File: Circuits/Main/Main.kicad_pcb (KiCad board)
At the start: 2 copper layers, 33 parts, among them CON1 BARREL_JACK, P1 led_stop, P10 toEncoder_MotorL, P11 toEncoder_motorR, P12 conn_resetButton, P13 conn_resetButton, P2 led_droite_face, P3 led_droite_cote, P4 led_gauche_face, P5 led_gauche_cote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

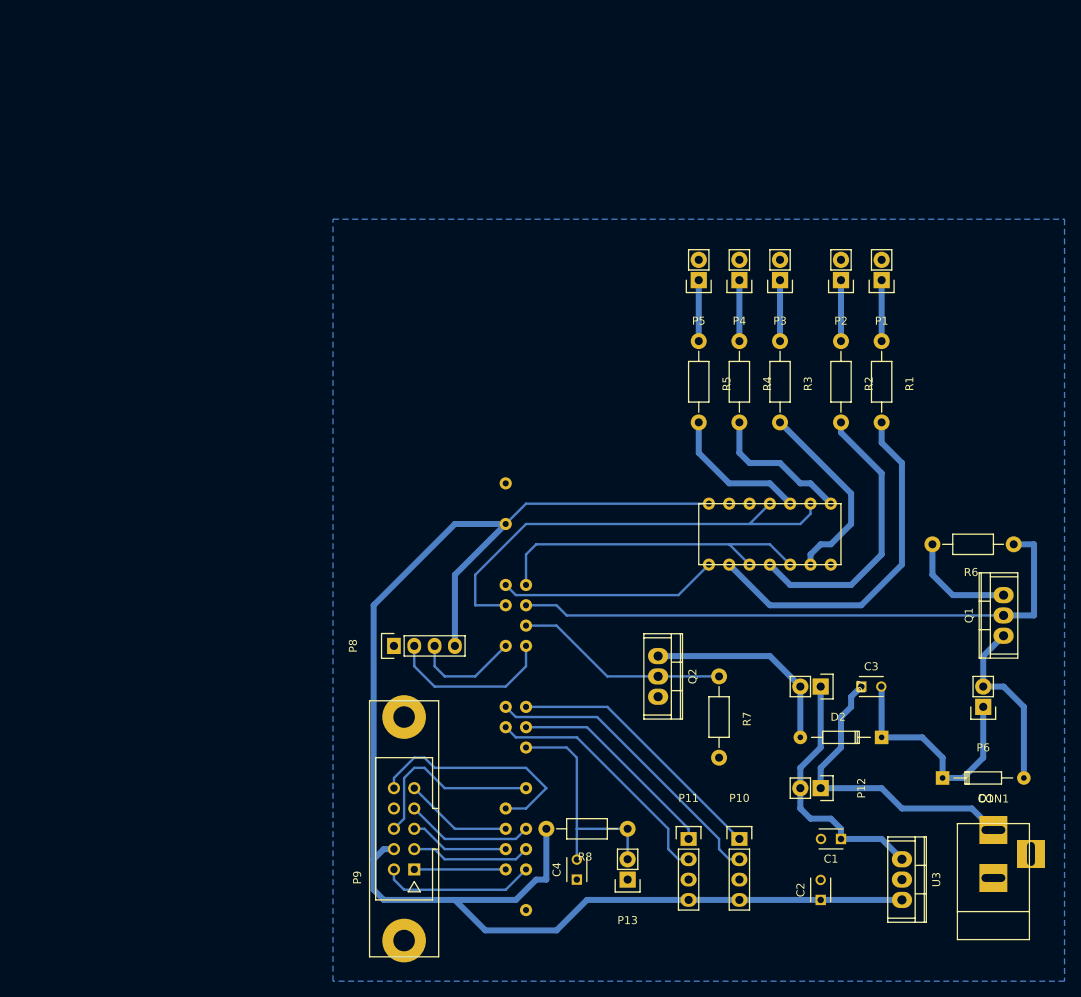
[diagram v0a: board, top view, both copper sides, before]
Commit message: Ajout de la carte principale (schemas + gerbers) et intégration
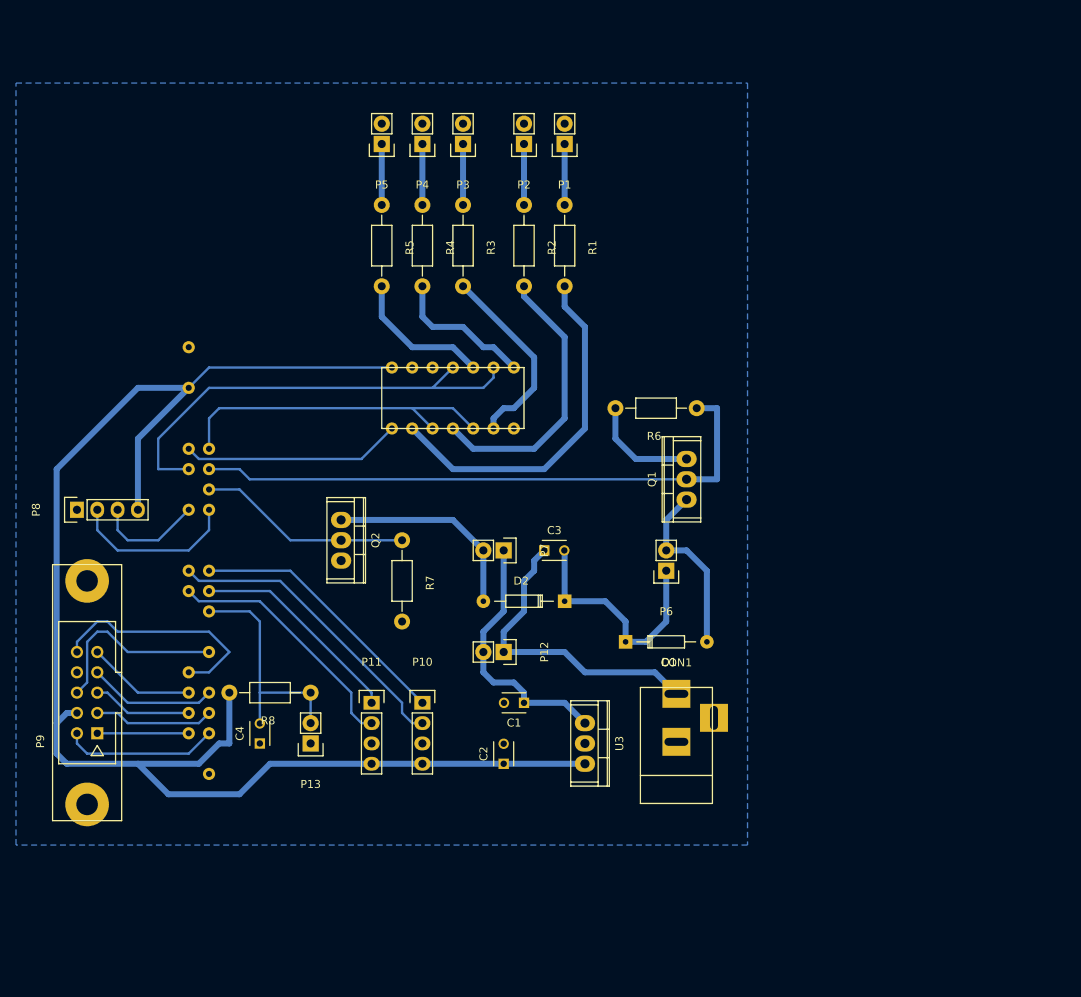
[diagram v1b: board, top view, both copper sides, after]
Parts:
- moved C3 43.1 mm to (92.5, 80.8)
- moved CON1 43.1 mm to (109.0, 104.9)
- moved D1 43.1 mm to (102.6, 92.2)
- moved D2 43.1 mm to (95.0, 87.1)
- moved P1 43.1 mm to (95.0, 30.0)
- moved P10 43.1 mm to (77.2, 99.8)
- moved P4 43.1 mm to (77.2, 30.0)
- moved P5 43.1 mm to (72.1, 30.0)
- moved Q1 43.1 mm to (110.2, 71.9)
- moved Q2 43.1 mm to (67.1, 79.5)
- moved R1 43.1 mm to (95.0, 37.6)
- moved R4 43.1 mm to (77.2, 37.6)
- moved R5 43.1 mm to (72.1, 37.6)
- moved R6 43.1 mm to (111.5, 63.0)
- moved P13 43.1 mm to (63.2, 104.9)
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
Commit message: Ameliorations cartes + rapport
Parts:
- P1: value led_stop -> toEncoder_MotorL; footprint Pin_Headers:Pin_Header_Straight_1x02 -> Pin_Headers:Pin_Header_Straight_1x04
- P10: value toEncoder_MotorL -> conn_moteur_gauche; footprint Pin_Headers:Pin_Header_Straight_1x04 -> Pin_Headers:Pin_Header_Straight_1x02
- P11: value toEncoder_motorR -> ultrasonicSensor
- P12: value conn_resetButton -> HE10-10; footprint Pin_Headers:Pin_Header_Straight_1x02 -> Connect:he10-10d
- P2: value led_droite_face -> led_stop
- P3: value led_droite_cote -> toEncoder_motorR; footprint Pin_Headers:Pin_Header_Straight_1x02 -> Pin_Headers:Pin_Header_Straight_1x04
- P4: value led_gauche_face -> led_droite_face
- P5: value led_gauche_cote -> led_droite_cote
- P6: value conn_moteur_droit -> led_gauche_face
- P7: value conn_moteur_gauche -> led_gauche_cote
- P8: value ultrasonicSensor -> conn_moteur_droit; footprint Pin_Headers:Pin_Header_Straight_1x04 -> Pin_Headers:Pin_Header_Straight_1x02
- P9: value HE10-10 -> conn_switchOnOff; footprint Connect:he10-10d -> Pin_Headers:Pin_Header_Straight_1x02
- U3: footprint Power_Integrations:TO-220 -> MES_EMPREINTES:voltageRegulator5v
- moved P6 86.3 mm to (42.5, 26.7), turned to 270 degrees
- moved P7 66.4 mm to (42.5, 31.8)
- moved P8 59.0 mm to (92.7, 69.2), turned to 270 degrees
- moved P11 53.3 mm to (42.5, 54.6), turned to 180 degrees
- moved P9 52.5 mm to (85.1, 81.9), turned to 270 degrees
- moved P12 45.6 mm to (43.8, 80.0), turned to 90 degrees
- moved P13 44.9 mm to (54.0, 61.0), turned to 90 degrees
- moved R8 41.9 mm to (56.5, 57.1)
- moved R6 41.7 mm to (78.1, 38.1), turned to 0 degrees
- moved C4 40.2 mm to (54.0, 64.8), turned to 0 degrees
- moved U3 39.8 mm to (60.3, 90.8), turned to 180 degrees
- moved D1 38.9 mm to (100.3, 53.3), turned to 90 degrees
- moved P3 35.1 mm to (71.8, 63.5), turned to 0 degrees
- moved Q1 34.4 mm to (95.9, 40.6)
- moved R4 32.1 mm to (47.0, 26.7), turned to 0 degrees
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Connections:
- C2 pad 1: 5v_Bat -> +BATT
- C2 pad 2: gnd -> batt
- C3 pad 1: +BATT -> 5v_Bat
- C3 pad 2: batt -> gnd
- P1 pad 1: Net-(P1-Pad1) -> toEncoder1B
- P1 pad 2: gnd -> toEncoder1A
- P10 pad 1: toEncoder1B -> batt
- P10 pad 2: toEncoder1A -> Net-(D2-Pad2)
- P11 pad 1: toEncoder2B -> gnd
- P11 pad 2: toEncoder2A -> echo
- P11 pad 3: gnd -> trig
- P12 pad 1: +BATT -> suiveur6
- P12 pad 2: batt -> suiveur7
- P3 pad 1: Net-(P3-Pad1) -> toEncoder2B
- P3 pad 2: gnd -> toEncoder2A
- P6 pad 1: batt -> Net-(P6-Pad1)
- P6 pad 2: Net-(D1-Pad2) -> gnd
- P7 pad 1: batt -> Net-(P7-Pad1)
- P7 pad 2: Net-(D2-Pad2) -> gnd
- P8 pad 1: gnd -> batt
- P8 pad 2: echo -> Net-(D1-Pad2)
- P9 pad 1: suiveur6 -> +BATT
- P9 pad 2: suiveur7 -> batt
- R1 pad 1: Net-(P1-Pad1) -> Net-(P2-Pad1)
- R2 pad 1: Net-(P2-Pad1) -> Net-(P4-Pad1)
- R3 pad 1: Net-(P3-Pad1) -> Net-(P5-Pad1)
- R4 pad 1: Net-(P4-Pad1) -> Net-(P6-Pad1)
- R5 pad 1: Net-(P5-Pad1) -> Net-(P7-Pad1)
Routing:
- net batt: track 62.5 -> 125.2 mm
- net Net-(R1-Pad2): track 44.6 -> 3.17 mm
- net cmd_moteur_droit: track 75.5 -> 36.9 mm
- net Net-(R2-Pad2): track 35.2 -> 3.17 mm
- net +BATT: track 38.6 -> 9.63 mm
- net 5v_Bat: track 192.2 -> 164.4 mm
- net toEncoder1A: track 37.8 -> 14.8 mm
- net toEncoder1B: track 33.5 -> 12.3 mm
- net Net-(R3-Pad2): track 24.3 -> 3.17 mm
- net Net-(D1-Pad2): track 22.4 -> 43.1 mm
- net Net-(U1-Pad13): track 57.5 -> 36.9 mm
- net toEncoder2A: track 31.2 -> 11.7 mm
- net toEncoder2B: track 26.9 -> 8.15 mm
- net toReset: track 29.8 -> 15.3 mm
- net Net-(U1-Pad12): track 42.0 -> 29.0 mm
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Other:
- net class Default: trace_width 0.75 -> 0.25
- net class highCurrent added: clearance 0.2, trace_width 0.7, via_dia 0.6, via_drill 0.4
